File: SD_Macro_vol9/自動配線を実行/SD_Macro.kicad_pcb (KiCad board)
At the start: 2 copper layers, 191.9 x 136.1 mm, 101 parts, among them J1 TRRS_MJ-4PP-9, SW1 SW_PUSH, SW10 SW_PUSH, SW11 SW_PUSH, SW12 SW_PUSH, SW13 SW_PUSH, SW14 SW_PUSH, SW15 SW_PUSH, SW16 SW_PUSH, SW17 SW_PUSH, SW18 SW_PUSH, SW19 SW_PUSH, SW2 SW_PUSH, SW20 SW_PUSH, SW21 SW_PUSH, SW22 SW_PUSH, SW23 Rotary_Encoder_Switch, SW24 SW_PUSH, SW25 SW_PUSH, SW26 SW_PUSH, SW27 SW_PUSH, SW28 SW_PUSH, SW29 SW_PUSH, SW3 SW_PUSH, SW30 SW_PUSH, SW31 SW_PUSH, SW32 SW_PUSH, SW33 SW_PUSH, SW34 SW_PUSH, SW4 SW_PUSH, SW5 SW_PUSH, SW6 SW_PUSH, SW7 SW_PUSH, SW8 SW_PUSH, SW9 SW_PUSH, U1 ProMicro

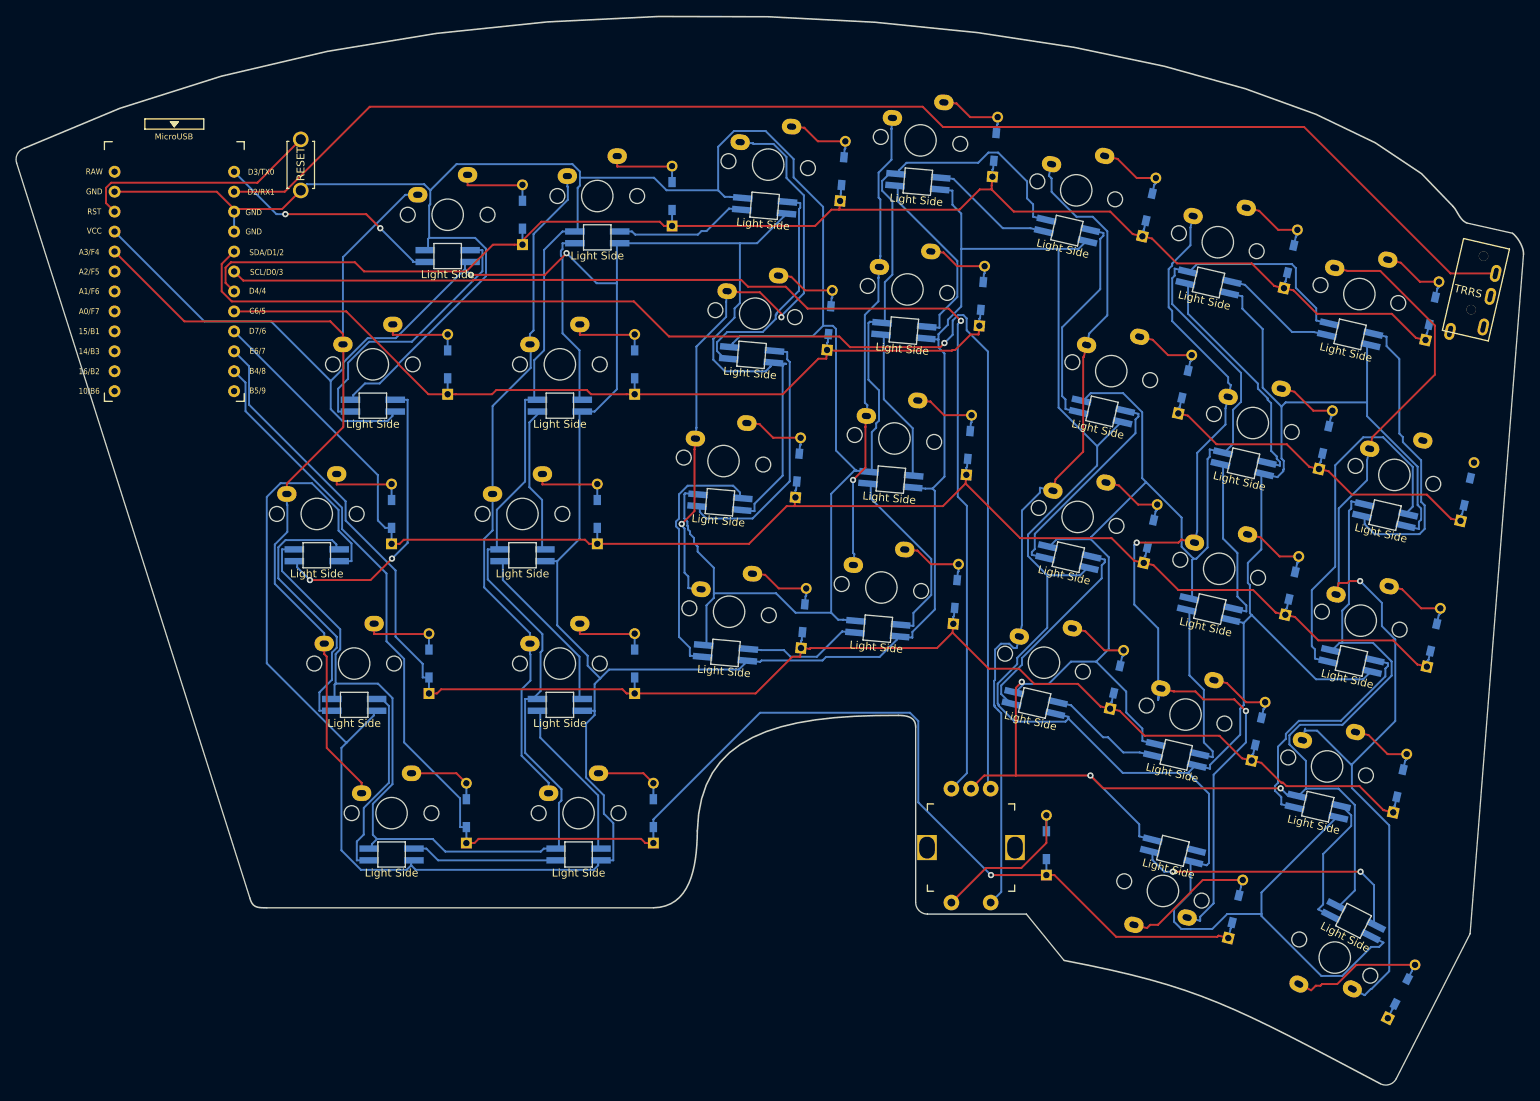
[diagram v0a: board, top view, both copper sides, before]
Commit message: ProMicro の表裏を変更
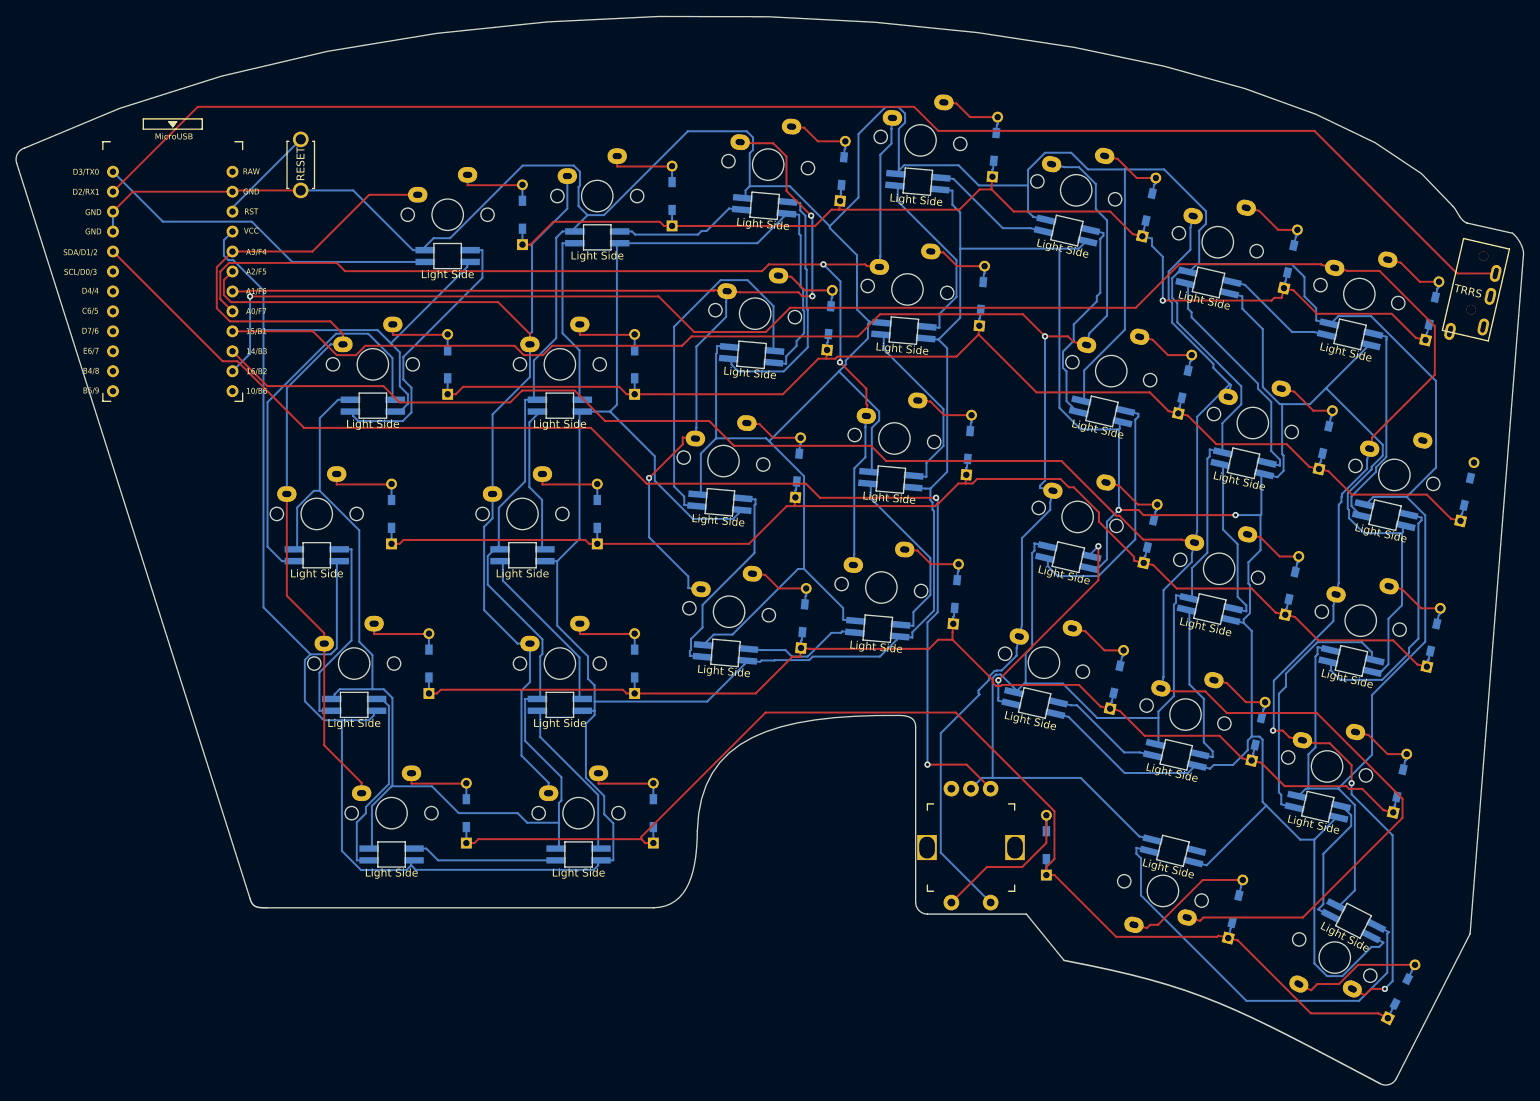
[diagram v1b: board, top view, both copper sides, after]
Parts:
- SW1, SW11, SW12, SW13, SW14, SW15, SW16, SW17, SW18, SW19, SW20, SW21, SW22, SW24, SW25, SW26, SW27, SW28, SW29, SW30, SW31, SW32, SW6, SW7, SW8, SW9: footprint kbd_SW:CherryMX_1u_solder -> kbd_SW:CherryMX_1u_solder_plateless
- SW10, SW33, SW5: footprint kbd_SW:CherryMX_1.25u_solder -> kbd_SW:CherryMX_1.25u_solder_plateless
- SW2: footprint kbd_SW:CherryMX_1.5u_solder -> kbd_SW:CherryMX_1.5u_solder_plateless
- SW3, SW4: footprint kbd_SW:CherryMX_1.75u_solder -> kbd_SW:CherryMX_1.75u_solder_plateless
- U1: footprint kbd:ProMicro_v3.5 -> kbd:ProMicro_v3.5_rev2
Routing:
- net RotaryB: track 156.3 -> 0.00 mm, vias 1 -> 0
- net Col5: track 120.9 -> 275.1 mm, vias 2 -> 0
- net Col6: track 130.6 -> 276.8 mm, vias 1 -> 4
- net Col4: track 108.1 -> 225.8 mm, vias 0 -> 1
- net Col3: track 59.3 -> 151.8 mm, vias 1 -> 2
- net Col2: track 79.7 -> 146.5 mm, vias 2 -> 3
- net Row3: track 204.0 -> 152.1 mm
- net GND: track 831.8 -> 879.1 mm, vias 3 -> 0
- net Col1: track 88.1 -> 134.0 mm
- net Row4: track 203.1 -> 158.6 mm, vias 1 -> 0
- net VCC: track 815.9 -> 775.3 mm
- net Row0: track 187.1 -> 148.8 mm, vias 0 -> 1
- net Row2: track 195.2 -> 162.8 mm
- net Net-(LED31-Pad1): track 35.6 -> 54.2 mm, vias 2 -> 0
- net Reset: track 30.8 -> 12.8 mm
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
